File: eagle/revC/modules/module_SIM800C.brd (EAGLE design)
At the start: 24.1 x 32.8 mm, 10 parts, among them IC1 SIM800C, X1 734120110

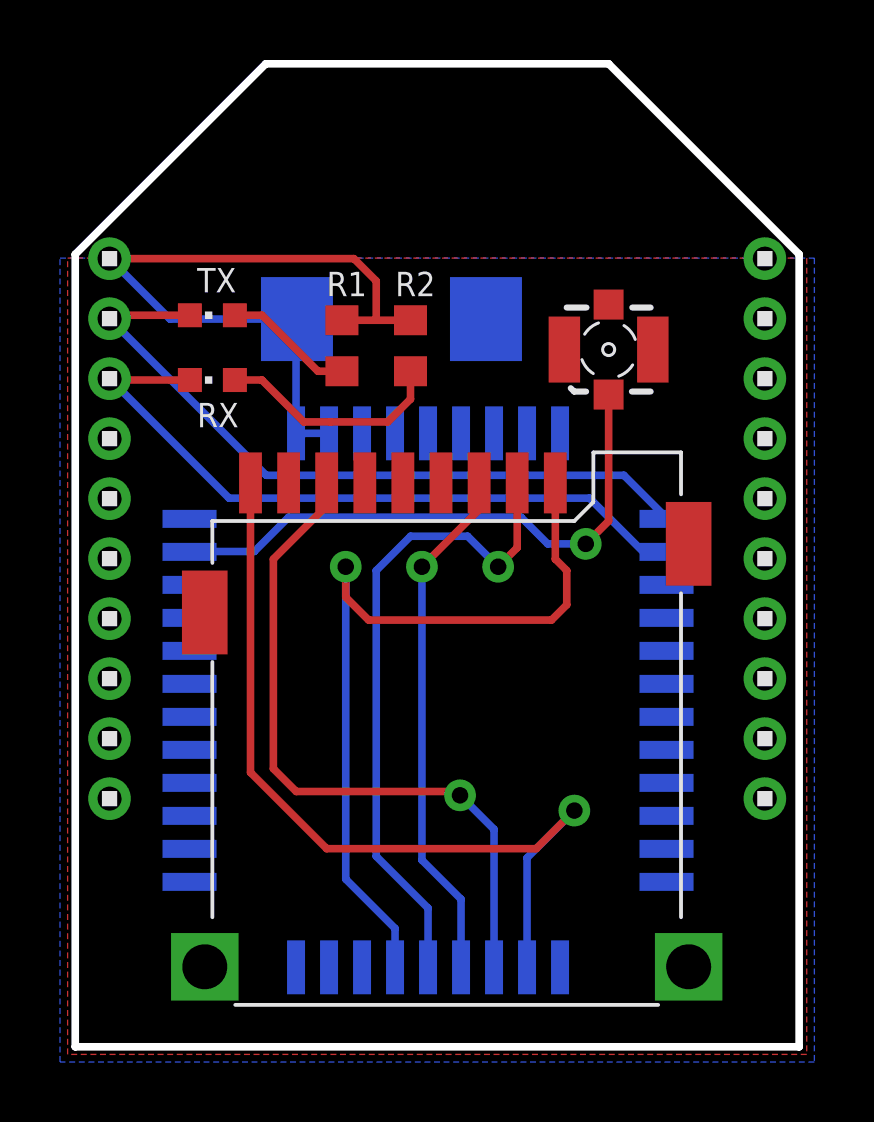
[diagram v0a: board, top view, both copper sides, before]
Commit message: [SIM800C] Added PWRKEY connection
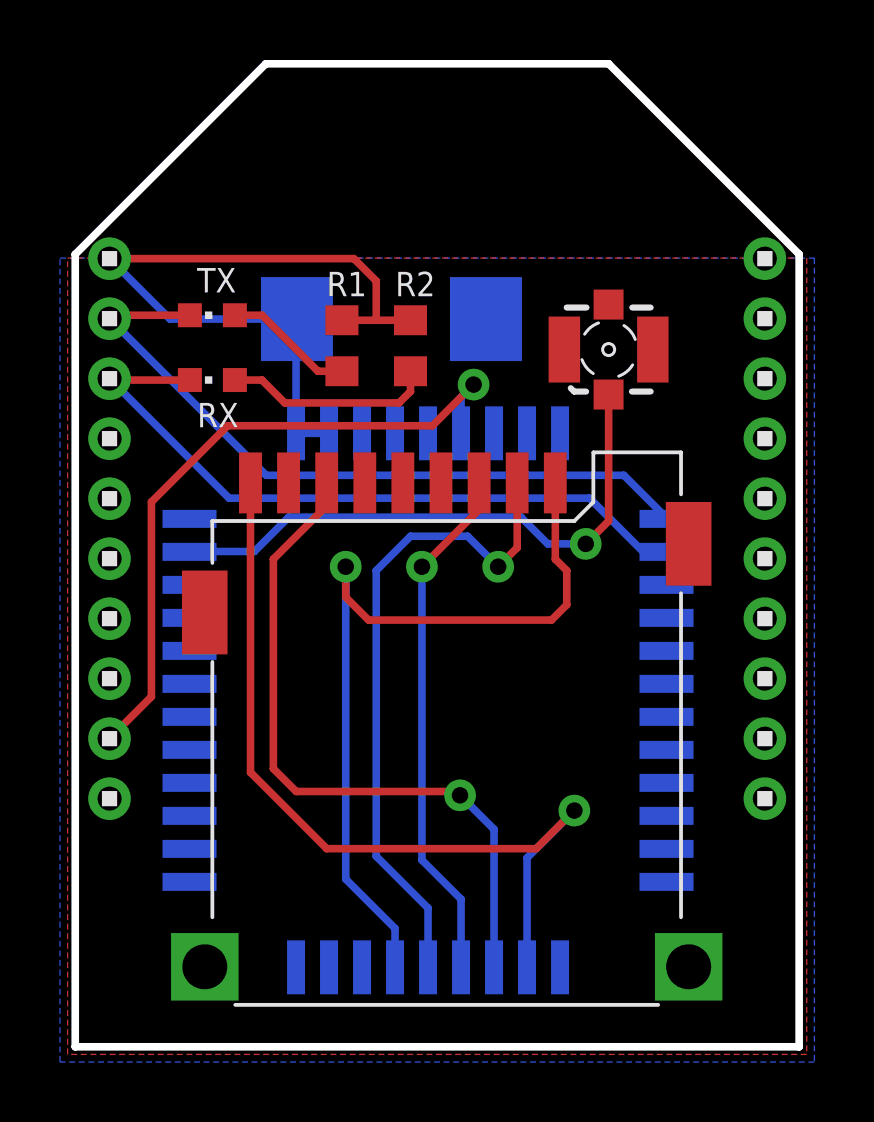
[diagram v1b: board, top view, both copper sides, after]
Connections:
- new net PWRKEY: IC1.39, LEFT1.9
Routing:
- net PWRKEY: track 0.00 -> 22.6 mm, vias 0 -> 1
- net N$3: track 7.68 -> 7.00 mm
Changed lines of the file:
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@@
 <contactref element="RX" pad="A"/>
 <wire x1="5.449" y1="22.352" x2="6.35" y2="22.352" width="0.254" layer="1"/>
-<wire x1="7.747" y1="20.955" x2="6.35" y2="22.352" width="0.254" layer="1"/>
-<wire x1="11.303" y1="22.645" x2="11.303" y2="21.717" width="0.254" layer="1"/>
-<wire x1="11.303" y1="21.717" x2="10.541" y2="20.955" width="0.254" layer="1"/>
-<wire x1="10.541" y1="20.955" x2="8.636" y2="20.955" width="0.254" layer="1"/>
-<wire x1="8.636" y1="20.955" x2="7.747" y2="20.955" width="0.254" layer="1"/>
+<wire x1="7.112" y1="21.59" x2="6.35" y2="22.352" width="0.254" layer="1"/>
+<wire x1="11.303" y1="22.645" x2="11.303" y2="21.971" width="0.254" layer="1"/>
+<wire x1="11.303" y1="21.971" x2="10.922" y2="21.59" width="0.254" layer="1"/>
+<wire x1="10.922" y1="21.59" x2="7.112" y2="21.59" width="0.254" layer="1"/>
 </signal>
 <signal name="SIM_DATA">
@@
 <wire x1="5.969" y1="9.271" x2="5.969" y2="18.923" width="0.254" layer="1"/>
 </signal>
+<signal name="PWRKEY">
+<contactref element="LEFT1" pad="9"/>
+<contactref element="IC1" pad="39"/>
+<wire x1="5.207" y1="20.828" x2="2.667" y2="18.288" width="0.254" layer="1"/>
+<wire x1="1.27" y1="10.399" x2="2.667" y2="11.796" width="0.254" layer="1"/>
+<wire x1="2.667" y1="11.796" x2="2.667" y2="18.288" width="0.254" layer="1"/>
+<wire x1="12.987" y1="20.574" x2="12.987" y2="21.78133125" width="0.254" layer="16"/>
+<wire x1="12.987" y1="21.78133125" x2="13.40666875" y2="22.201" width="0.254" layer="16"/>
+<via x="13.40666875" y="22.201" extent="1-16" drill="0.55"/>
+<wire x1="13.40666875" y1="22.201" x2="12.03366875" y2="20.828" width="0.254" layer="1"/>
+<wire x1="12.03366875" y1="20.828" x2="5.207" y2="20.828" width="0.254" layer="1"/>
+</signal>
 </signals>

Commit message: [SIM800C] Fixed incorrect SIM slot wiring
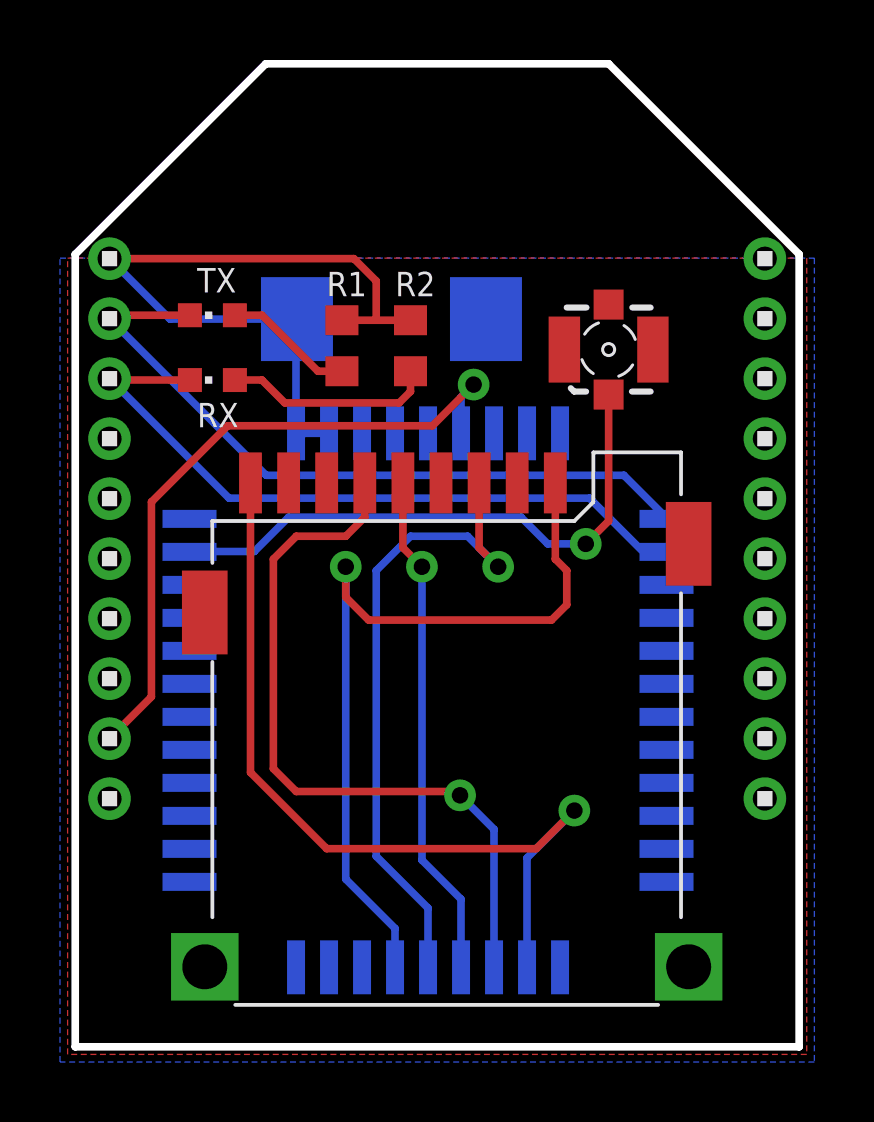
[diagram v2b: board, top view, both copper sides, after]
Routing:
- net SIM_DATA: track 23.1 -> 24.6 mm
- net SIM_CLK: track 17.5 -> 17.0 mm
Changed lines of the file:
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@@
 <contactref element="IC1" pad="15"/>
 <via x="12.954" y="8.509" extent="1-16" drill="0.55"/>
-<wire x1="8.509" y1="18.161" x2="6.731" y2="16.383" width="0.254" layer="1"/>
+<wire x1="7.493" y1="17.145" x2="6.731" y2="16.383" width="0.254" layer="1"/>
 <wire x1="7.493" y1="8.636" x2="12.827" y2="8.636" width="0.254" layer="1"/>
 <wire x1="12.827" y1="8.636" x2="12.954" y2="8.509" width="0.254" layer="1"/>
@@
 <wire x1="6.731" y1="9.398" x2="7.493" y2="8.636" width="0.254" layer="1"/>
 <contactref element="U$2" pad="P$7"/>
-<wire x1="8.509" y1="18.923" x2="8.509" y2="18.161" width="0.254" layer="1"/>
+<wire x1="9.779" y1="18.923" x2="9.779" y2="17.78" width="0.254" layer="1"/>
+<wire x1="9.779" y1="17.78" x2="9.144" y2="17.145" width="0.254" layer="1"/>
+<wire x1="9.144" y1="17.145" x2="7.493" y2="17.145" width="0.254" layer="1"/>
 <wire x1="14.087" y1="2.774" x2="14.087" y2="7.376" width="0.254" layer="16"/>
 <wire x1="14.087" y1="7.376" x2="12.954" y2="8.509" width="0.254" layer="16"/>
@@
 <wire x1="12.987" y1="5.047" x2="11.684" y2="6.35" width="0.254" layer="16"/>
 <via x="11.684" y="16.129" extent="1-16" drill="0.55"/>
-<wire x1="13.589" y1="18.034" x2="11.684" y2="16.129" width="0.254" layer="1"/>
+<wire x1="11.049" y1="16.764" x2="11.684" y2="16.129" width="0.254" layer="1"/>
 <wire x1="11.684" y1="6.35" x2="11.684" y2="16.129" width="0.254" layer="16"/>
 <contactref element="U$2" pad="P$3"/>
-<wire x1="13.589" y1="18.923" x2="13.589" y2="18.034" width="0.254" layer="1"/>
+<wire x1="11.049" y1="18.923" x2="11.049" y2="16.764" width="0.254" layer="1"/>
 </signal>
 <signal name="SIM_RST">
@@
 <wire x1="13.208" y1="17.145" x2="14.224" y2="16.129" width="0.254" layer="16"/>
 <contactref element="U$2" pad="P$2"/>
-<wire x1="14.859" y1="18.923" x2="14.859" y2="16.764" width="0.254" layer="1"/>
-<wire x1="14.859" y1="16.764" x2="14.224" y2="16.129" width="0.254" layer="1"/>
+<wire x1="13.589" y1="18.923" x2="13.589" y2="16.764" width="0.254" layer="1"/>
+<wire x1="13.589" y1="16.764" x2="14.224" y2="16.129" width="0.254" layer="1"/>
 </signal>
 <signal name="SIM_VDD">

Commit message: [SIM800] Added SIM detection pullup
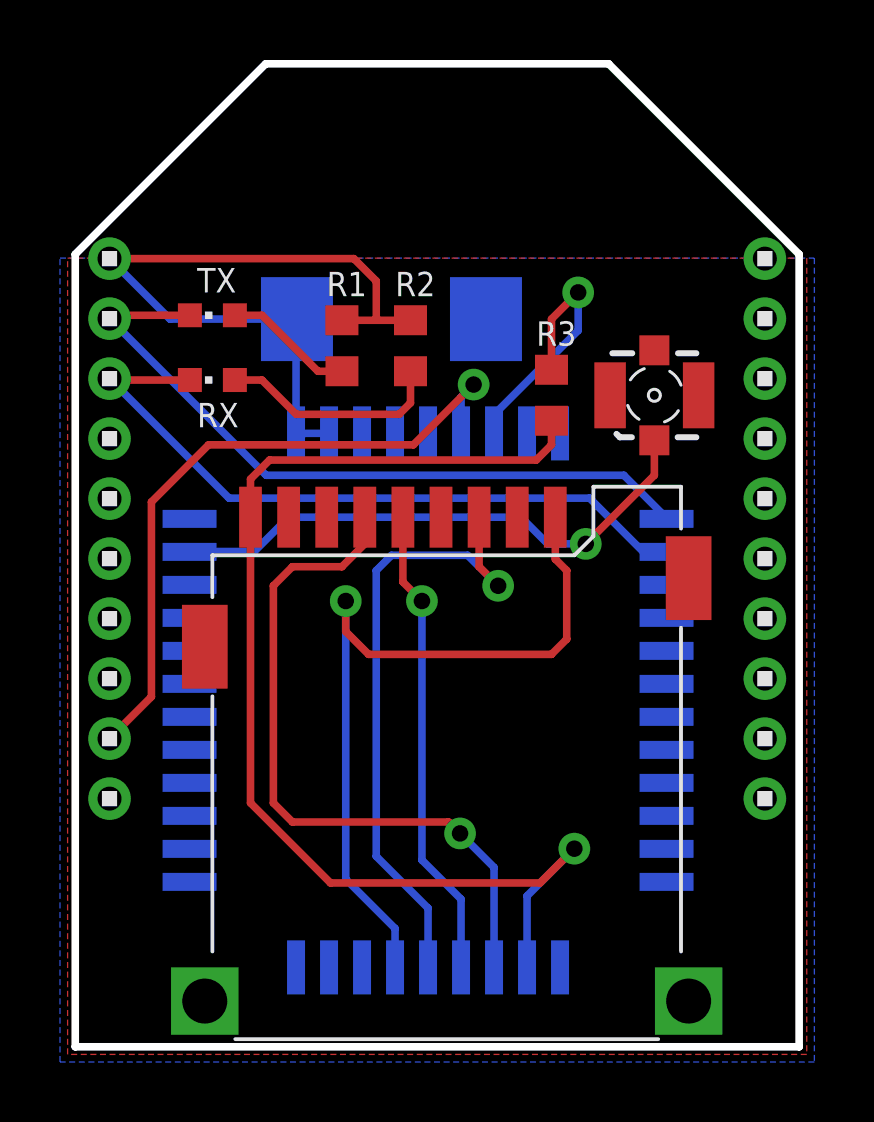
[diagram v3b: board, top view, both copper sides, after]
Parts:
- added R3: 4k7, rcl:R0603
- moved X1 2.16 mm to (19.4, 21.8)
- moved U$2 1.14 mm to (12.3, 8.51)
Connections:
- new net VDD_EXT: IC1.40, R3.2
- net SIM_DET: now also R3.1
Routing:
- net SIM_DET: track 27.9 -> 39.1 mm
- net VDD_EXT: track 0.00 -> 8.81 mm, vias 0 -> 1
- net SIM_DATA: track 24.6 -> 23.3 mm
- net SIM_VDD: track 27.2 -> 26.0 mm
- net SIM_CLK: track 17.0 -> 15.8 mm
- net N$1: track 19.3 -> 18.5 mm
- net SIM_RST: track 22.0 -> 21.2 mm
- net N$3: track 7.00 -> 7.54 mm
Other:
- board text added: "R3"

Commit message: Replaced modules with library parts
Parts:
- IC1: device sim800c:SIM800C -> RadioShield:SIM800C
- U$2: device con-sim:115Q-BCA0 -> RadioShield:115Q-BCA0
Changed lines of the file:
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@@
 <?xml version="1.0" encoding="utf-8"?>
 <!DOCTYPE eagle SYSTEM "eagle.dtd">
-<eagle version="9.0.1">
+<eagle version="9.4.1">
 <drawing>
 <settings>
@@
 <wire x1="24.257" y1="26.543" x2="24.257" y2="0.127" width="0.254" layer="20"/>
 <wire x1="24.257" y1="0.127" x2="0.127" y2="0.127" width="0.254" layer="20"/>
-<text x="12.192" y="30.48" size="1.524" layer="51" font="vector" ratio="15" rot="SR0" align="center">SIM800C</text>
+<text x="12.192" y="30.48" size="1.778" layer="51" ratio="15" rot="SR0" align="center">SIM800C</text>
 <text x="5.461" y="25.4" size="0.8128" layer="52" font="vector" ratio="12" rot="SR0" align="center">+</text>
 <text x="5.842" y="21.971" size="0.8128" layer="126" font="vector" ratio="12" rot="SMR0">C1</text>
@@
 <param name="checkStop" value="0"/>
 <param name="checkValues" value="0"/>
+<param name="checkNames" value="1"/>
+<param name="checkWireStubs" value="1"/>
+<param name="checkPolygonWidth" value="0"/>
 <param name="useDiameter" value="13"/>
 <param name="maxErrors" value="50"/>
@@
 </autorouter>
 <elements>
-<element name="LEFT1" library="headers(2mm)" package="1X10" value="1X10" x="1.27" y="17.399" rot="R270"/>
-<element name="RIGHT1" library="headers(2mm)" package="1X10" value="1X10" x="23.114" y="17.399" rot="R270"/>
+<element name="LEFT1" library="headers(2mm)" package="1X10" value="1X10" x="1.27" y="17.399" smashed="yes" rot="R270"/>
+<element name="RIGHT1" library="headers(2mm)" package="1X10" value="1X10" x="23.114" y="17.399" smashed="yes" rot="R270"/>
 <element name="X1" library="con-coax" library_urn="urn:adsk.eagle:library:133" package="734120110" package3d_urn="urn:adsk.eagle:package:6199/1" value="734120110" x="19.431" y="21.844" smashed="yes"/>
-<element name="IC1" library="sim800c" package="SIM800C" value="SIM800C" x="11.887" y="11.674" smashed="yes" rot="MR0">
-<attribute name="3D_PACKAGE" value="" x="11.887" y="11.674" size="1.778" layer="28" rot="MR0" display="off"/>
-<attribute name="ALLIED_NUMBER" value="" x="11.887" y="11.674" size="1.778" layer="28" rot="MR0" display="off"/>
-<attribute name="DESCRIPTION" value="Quad-band GSM/GPRS wireless module" x="11.887" y="11.674" size="1.778" layer="28" rot="MR0" display="off"/>
-<attribute name="HEIGHT" value="mm" x="11.887" y="11.674" size="1.778" layer="28" rot="MR0" display="off"/>
-<attribute name="MANUFACTURER_NAME" value="SIMCOM" x="11.887" y="11.674" size="1.778" layer="28" rot="MR0" display="off"/>
-<attribute name="MANUFACTURER_PART_NUMBER" value="sim800c" x="11.887" y="11.674" size="1.778" layer="28" rot="MR0" display="off"/>
-<attribute name="OTHER_PART_NUMBER" value="" x="11.887" y="11.674" size="1.778" layer="28" rot="MR0" display="off"/>
-<attribute name="RS_PART_NUMBER" value="" x="11.887" y="11.674" size="1.778" layer="28" rot="MR0" display="off"/>
-<attribute name="SUPPLIER_NAME" value="RS" x="11.887" y="11.674" size="1.778" layer="28" rot="MR0" display="off"/>
+<element name="IC1" library="RadioShield" package="SIM800C" value="SIM800C" x="11.887" y="11.674" smashed="yes" rot="MR0">
 <attribute name="VALUE" x="12.120659375" y="11.722640625" size="0.8128" layer="52" font="vector" ratio="12" rot="SMR0" align="center"/>
 </element>
-<element name="R1" library="rcl" library_urn="urn:adsk.eagle:library:334" package="R0603" package3d_urn="urn:adsk.eagle:package:23555/2" value="1k" x="9.017" y="23.495" smashed="yes" rot="R90">
+<element name="R1" library="rcl" library_urn="urn:adsk.eagle:library:334" package="R0603" package3d_urn="urn:adsk.eagle:package:23555/3" value="1k" x="9.017" y="23.495" smashed="yes" rot="R90">
 <attribute name="NAME" x="8.509" y="25.146" size="0.8128" layer="25" font="vector" ratio="12" rot="SR0"/>
 <attribute name="SPICEPREFIX" value="R" x="9.017" y="23.495" size="1.778" layer="27" rot="R90" display="off"/>
 </element>
-<element name="R2" library="rcl" library_urn="urn:adsk.eagle:library:334" package="R0603" package3d_urn="urn:adsk.eagle:package:23555/2" value="1k" x="11.303" y="23.495" smashed="yes" rot="R90">
+<element name="R2" library="rcl" library_urn="urn:adsk.eagle:library:334" package="R0603" package3d_urn="urn:adsk.eagle:package:23555/3" value="1k" x="11.303" y="23.495" smashed="yes" rot="R90">
 <attribute name="NAME" x="10.795" y="25.146" size="0.8128" layer="25" font="vector" ratio="12" rot="SR0"/>
 <attribute name="SPICEPREFIX" value="R" x="11.303" y="23.495" size="1.778" layer="27" rot="R90" display="off"/>
@@
 <attribute name="VALUE" x="5.969" y="24.257" size="1.27" layer="27" rot="R180"/>
 </element>
-<element name="C1" library="rcl" library_urn="urn:adsk.eagle:library:334" package="SMC_D" package3d_urn="urn:adsk.eagle:package:23434/1" value="470uF" x="10.668" y="24.384" smashed="yes" rot="MR180">
+<element name="C1" library="rcl" library_urn="urn:adsk.eagle:library:334" package="SMC_D" package3d_urn="urn:adsk.eagle:package:25923/2" value="470uF" x="10.668" y="24.384" smashed="yes" rot="MR180">
 <attribute name="NAME" x="5.842" y="21.971" size="0.8128" layer="26" font="vector" ratio="12" rot="SMR0"/>
 <attribute name="SPICEPREFIX" value="C" x="10.668" y="24.384" size="0.8128" layer="28" font="vector" ratio="12" rot="MR180" display="off"/>
 </element>
-<element name="U$2" library="con-sim" package="115Q-BCA0" value="115Q-BCA0" x="12.319" y="8.509"/>
-<element name="R3" library="rcl" library_urn="urn:adsk.eagle:library:334" package="R0603" package3d_urn="urn:adsk.eagle:package:23555/2" value="4k7" x="16.002" y="21.844" smashed="yes" rot="R90">
+<element name="U$2" library="RadioShield" package="115Q-BCA0" value="115Q-BCA0" x="12.319" y="8.509" smashed="yes"/>
+<element name="R3" library="rcl" library_urn="urn:adsk.eagle:library:334" package="R0603" package3d_urn="urn:adsk.eagle:package:23555/3" value="4k7" x="16.002" y="21.844" smashed="yes" rot="R90">
 <attribute name="NAME" x="15.494" y="23.495" size="0.8128" layer="25" font="vector" ratio="12"/>
 <attribute name="SPICEPREFIX" value="R" x="16.002" y="21.844" size="1.778" layer="27" rot="R90" display="off"/>
@@
 </signal>
 </signals>
+<mfgpreviewcolors>
+<mfgpreviewcolor name="soldermaskcolor" color="0xC8008000"/>
+<mfgpreviewcolor name="silkscreencolor" color="0xFFFEFEFE"/>
+<mfgpreviewcolor name="backgroundcolor" color="0xFF282828"/>
+<mfgpreviewcolor name="coppercolor" color="0xFFFFBF00"/>
+<mfgpreviewcolor name="substratecolor" color="0xFF786E46"/>
+</mfgpreviewcolors>
 </board>
 </drawing>
